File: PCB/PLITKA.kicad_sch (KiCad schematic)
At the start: 54 parts, among them SW1 MX_SW_HS, SW10 MX_SW_HS, SW11 MX_SW_HS, SW12 MX_SW_HS, SW13 MX_SW_HS, SW14 MX_SW_HS, SW15 MX_SW_HS, SW16 MX_SW_HS, SW17 MX_SW_HS, SW2 MX_SW_HS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

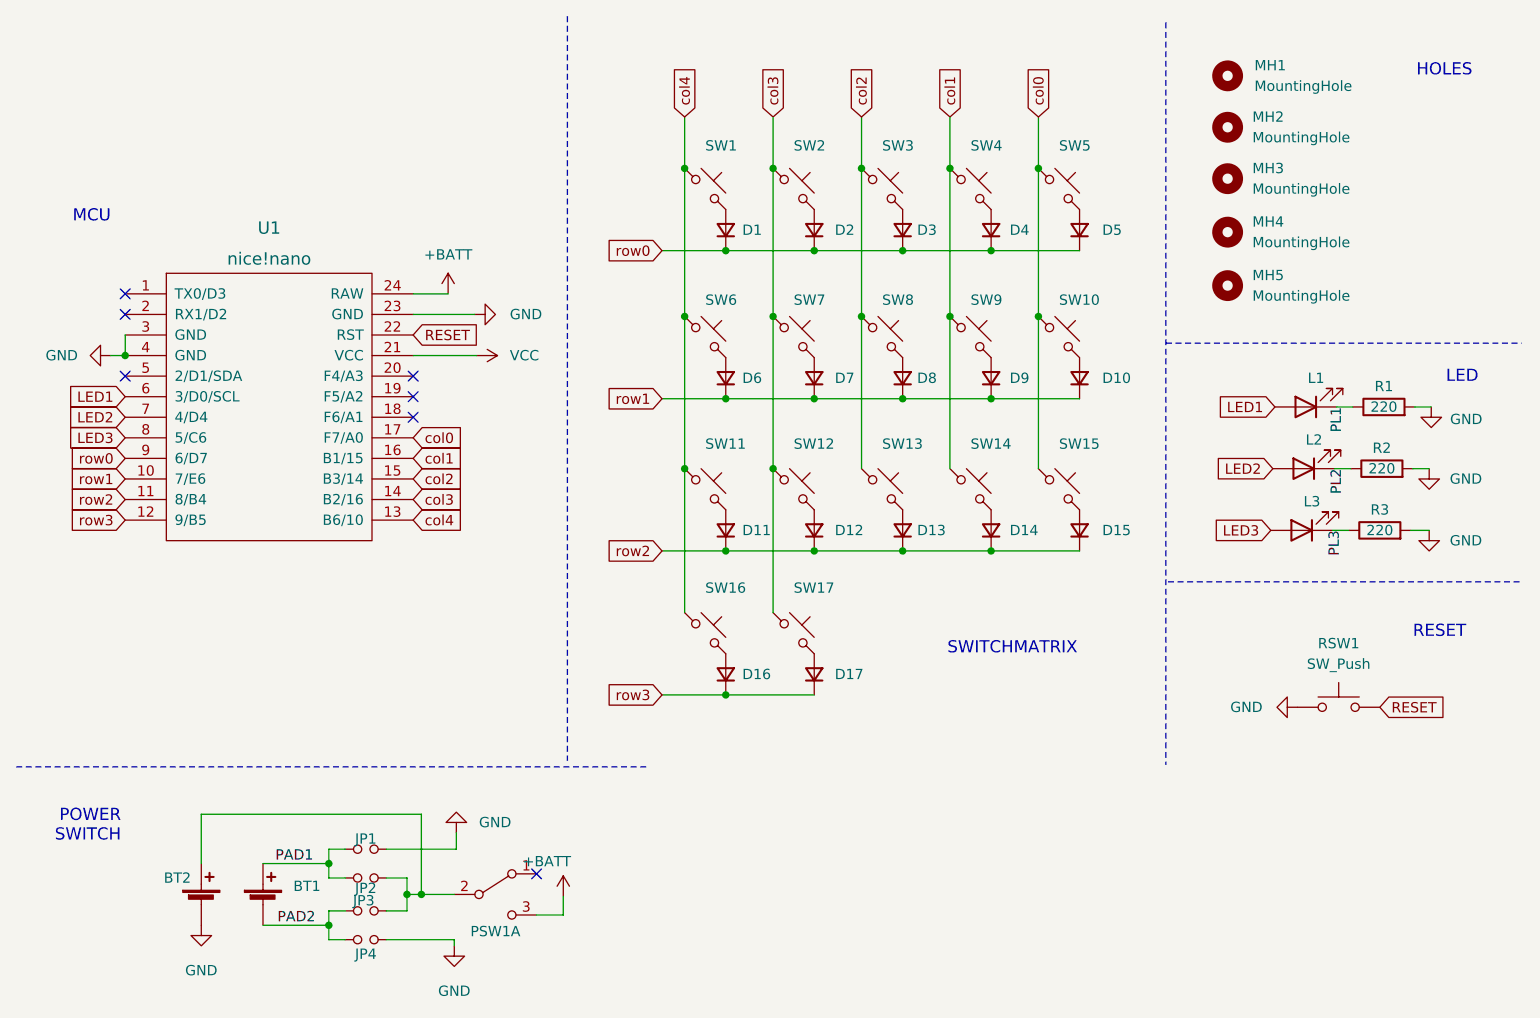
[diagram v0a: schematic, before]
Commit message: Led removal
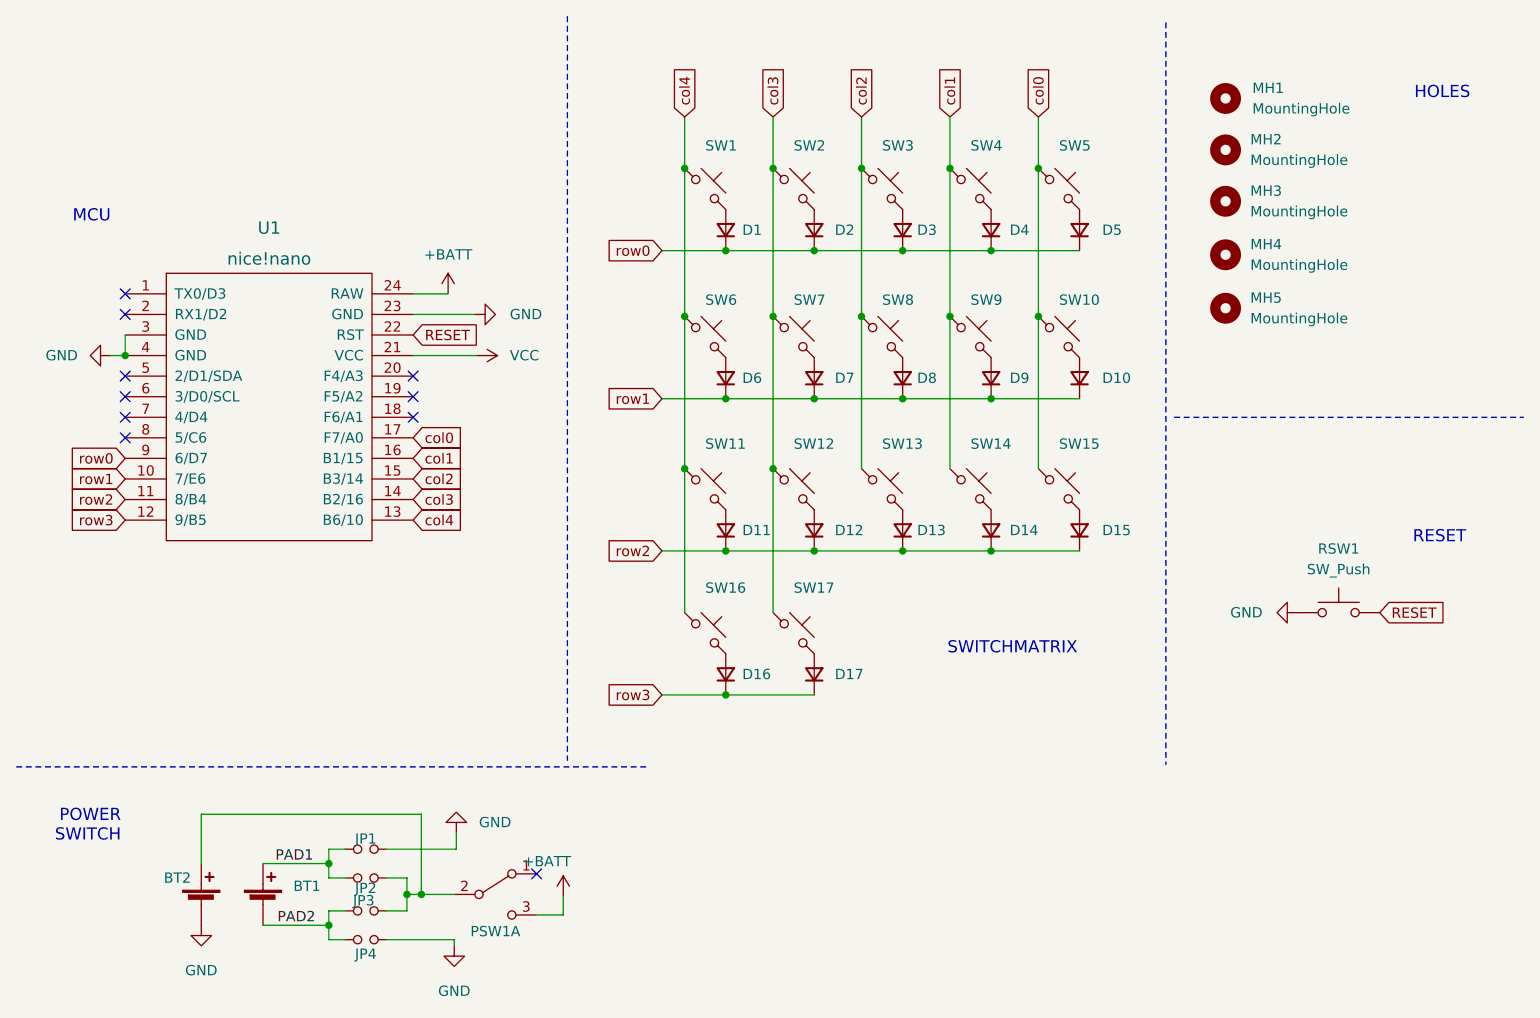
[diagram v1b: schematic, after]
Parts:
- removed L1, L2, L3: LED, PLITKA:LED_3mm_reversible, symbol Device:LED
- removed R1, R2, R3: 220, PLITKA:R_1206_DoubleSided, symbol Device:R
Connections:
- net LED1: no longer names the net of U1.6 (3/D0/SCL)
- net LED2: no longer names the net of U1.7 (4/D4)
- net LED3: no longer names the net of U1.8 (5/C6)
- no-connect marks 7 -> 10
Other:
- note removed: "LED"
- moved on the sheet: MH1, MH2, MH3, MH4, MH5, RSW1
